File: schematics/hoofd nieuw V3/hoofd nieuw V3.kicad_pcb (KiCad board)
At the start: 2 copper layers, 175 x 75 mm, 42 parts, among them J1 Conn_01x04_Pin, J2 Conn_01x02_Pin, J3 SFR02, J4 Conn_01x03_Pin, J5 Conn_01x01, J6 Conn_01x01, J7 Conn_01x01, J8 Conn_01x01, U1 ATtiny402-SS, Y1 ECS-2333MV-100-BN-TR

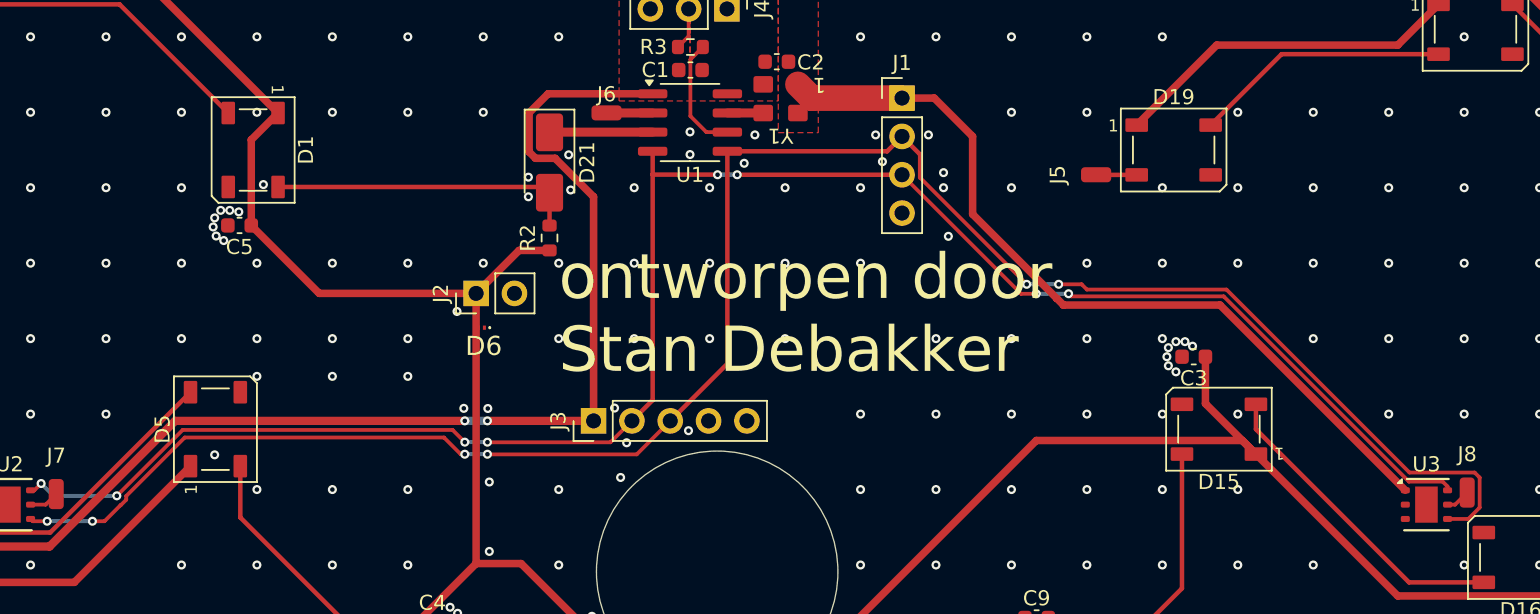
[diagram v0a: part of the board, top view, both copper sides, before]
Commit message: voeg nog ESD bescherming toe aan nieuw hoofd V3
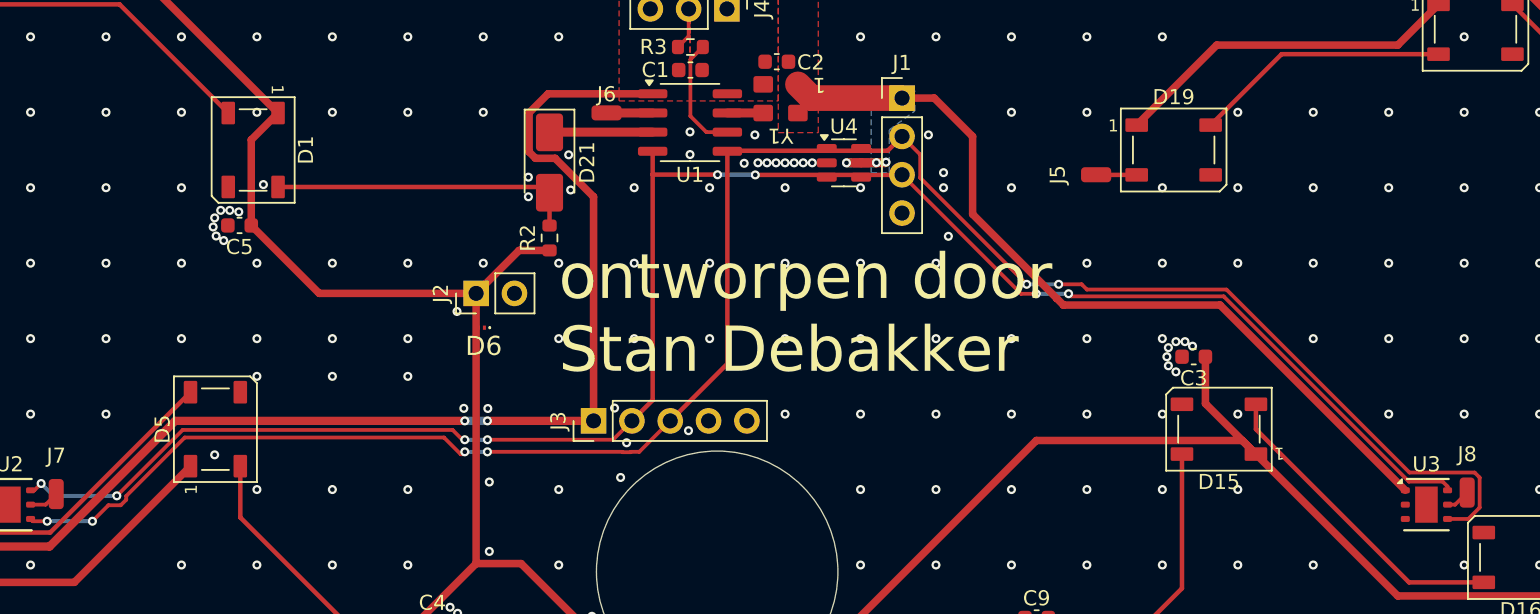
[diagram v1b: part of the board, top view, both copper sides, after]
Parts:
- added U4: USBLC6-2SC6, Package_TO_SOT_SMD:SOT-23-6, F.Cu at (139.9, 43.4)
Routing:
- net +3.3V: track 141.3 -> 145.9 mm, vias 2 -> 5
- net GND: vias 394 -> 402
- added copper zone on B.Cu, net +3.3V
